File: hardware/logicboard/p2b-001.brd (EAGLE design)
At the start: 91 x 90 mm, 57 parts, among them IC1 74LS06N, IC2 4066N, J1 MKR, J2 GPIO, J3 Vcc, J4 RLY, J5 SPI, J7 DIN5, J8 DIN5, J9 DIN5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

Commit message: Added relay pad.
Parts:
- added A, B: (no value), wirepad:SMD1,27-2,54
- moved C1 1.00 mm to (26.0, 24.0)
- moved C2 1.00 mm to (26.0, 28.0)
- moved C3 1.00 mm to (26.0, 31.0)
- moved C4 1.00 mm to (26.0, 34.0)
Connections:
- net VOUTRAW: now also B.1
- net VOUTRAW2: now also A.1
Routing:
- net VIN: track 81.9 -> 142.1 mm, vias 6 -> 7
- net DTCT0: track 71.1 -> 112.8 mm, vias 3 -> 2
- net LED1: track 87.4 -> 122.5 mm, vias 5 -> 4
- net SCL: track 150.7 -> 179.9 mm, vias 7 -> 3
- net THS: track 108.5 -> 129.8 mm, vias 0 -> 3
- net MTSND: track 78.8 -> 98.6 mm, vias 1 -> 0
- net DTCT2: track 127.7 -> 108.9 mm, vias 2 -> 3
- net GPIO1: track 127.0 -> 108.8 mm, vias 2 -> 6
- net MISND: track 111.9 -> 94.0 mm, vias 2 -> 6
- net DTCT3: track 127.7 -> 109.9 mm
- net RX: track 83.1 -> 67.3 mm, vias 2 -> 3
- net D7GATE: track 139.7 -> 125.0 mm, vias 0 -> 4
- net MOSND: track 67.0 -> 52.5 mm, vias 0 -> 3
- net GPIO0: track 109.1 -> 94.8 mm, vias 2 -> 3
- net VCC: track 310.8 -> 324.5 mm, vias 4 -> 3
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
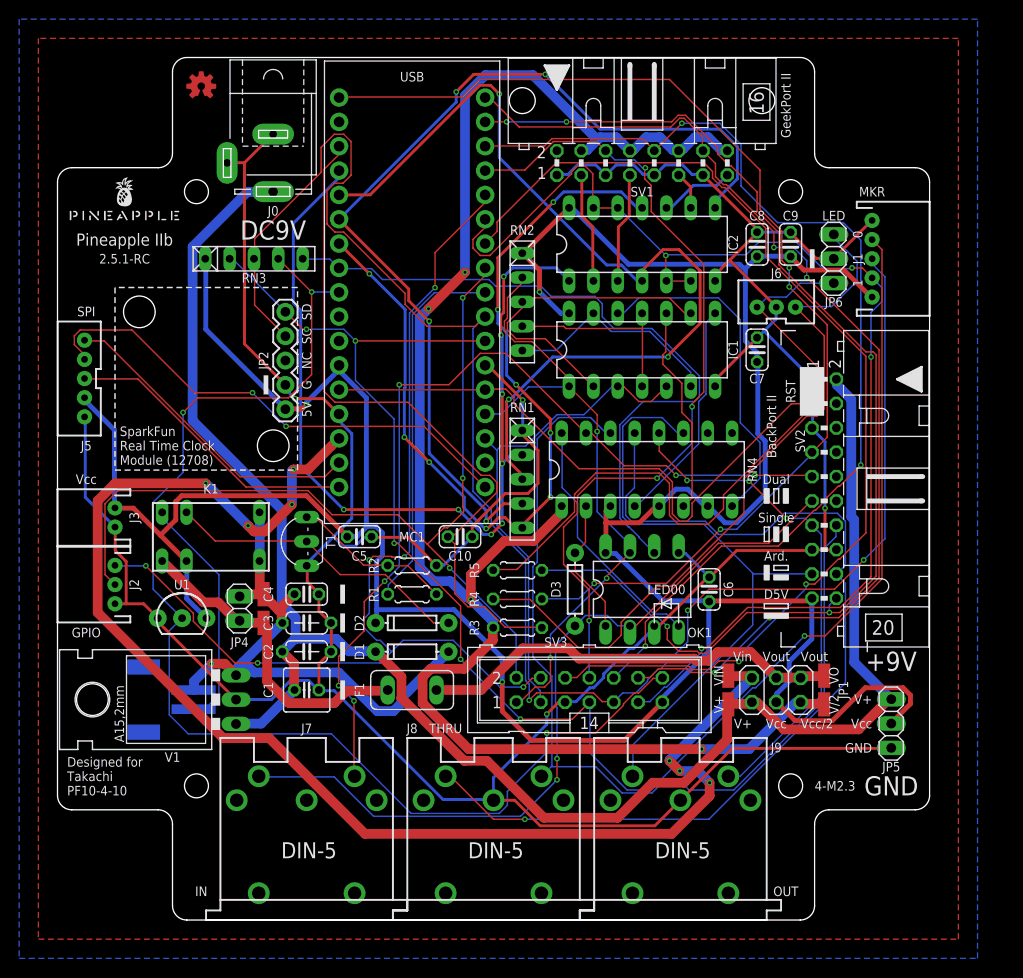
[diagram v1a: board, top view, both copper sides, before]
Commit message: Replaced ML connector with header pins.
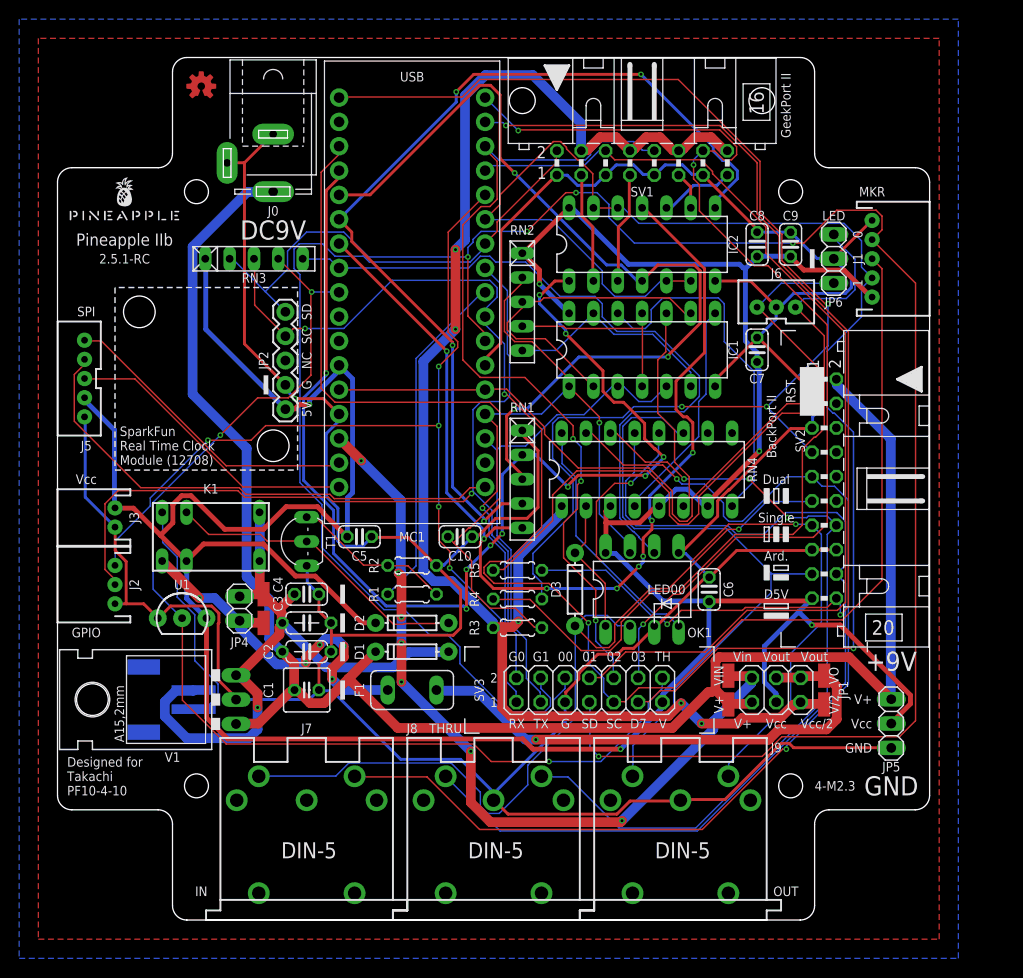
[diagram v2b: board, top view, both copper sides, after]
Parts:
- SV3: device con-ml:ML14 -> pinhead:2X07
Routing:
- net VIN: track 142.1 -> 83.7 mm
- net GND: track 375.9 -> 425.9 mm, vias 4 -> 1
- net VCC: track 324.5 -> 353.0 mm, vias 3 -> 5
- net ANLG0: track 93.8 -> 121.8 mm, vias 8 -> 10
- net SDA: track 167.5 -> 190.6 mm, vias 6 -> 5
- net D7GATE: track 125.0 -> 146.9 mm, vias 4 -> 1
- net DTCT2: track 108.9 -> 88.4 mm
- net MISND: track 94.0 -> 114.5 mm, vias 6 -> 2
- net DTCT1: track 85.9 -> 106.2 mm, vias 4 -> 0
- net SCL: track 179.9 -> 160.4 mm
- net MOSND: track 52.5 -> 71.6 mm, vias 3 -> 2
- net ANLG3: track 91.2 -> 108.5 mm, vias 9 -> 8
- net MTSND: track 98.6 -> 83.7 mm, vias 0 -> 3
- net LED0: track 116.3 -> 130.8 mm, vias 4 -> 3
- net VCC/2: track 172.4 -> 159.7 mm, vias 4 -> 5
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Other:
- board text added: "00"
- board text added: "01"
- board text added: "02"
- board text added: "03"
- board text added: "2"
- board text added: "D7"
- board text added: "G0"
- board text added: "G1"
- board text added: "RX"
- board text added: "TH"
- board text added: "TX"
- board text added: "V"

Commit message: Position of Tr.
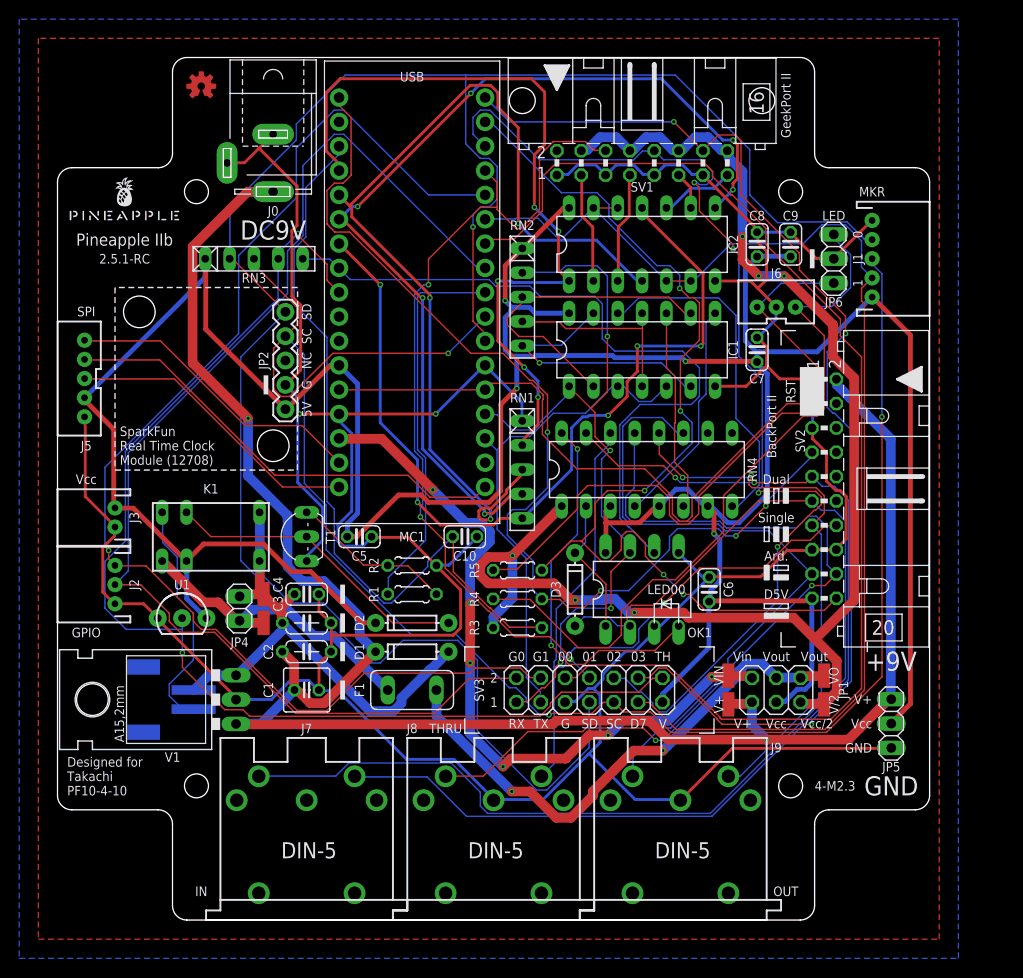
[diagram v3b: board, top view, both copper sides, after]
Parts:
- moved RN1 1.00 mm to (48.5, 47.0)
- moved C10 0.50 mm to (42.5, 40.0)
- moved RN2 0.50 mm to (48.5, 65.0)
- moved T1 0.50 mm to (26.0, 40.0)
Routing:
- net ANLG0: track 121.8 -> 81.4 mm, vias 10 -> 5
- net MIRTN: track 91.3 -> 123.7 mm, vias 1 -> 0
- net GPIO0: track 97.5 -> 127.5 mm, vias 1 -> 0
- net SDA: track 190.6 -> 216.7 mm, vias 5 -> 1
- net DTCT2: track 88.4 -> 114.0 mm, vias 3 -> 4
- net DTCT0: track 103.5 -> 126.7 mm
- net LED0: track 130.8 -> 108.2 mm, vias 3 -> 4
- net D7GATE: track 146.9 -> 124.6 mm, vias 1 -> 0
- net GPIO1: track 109.3 -> 130.7 mm, vias 5 -> 1
- net SCL: track 160.4 -> 180.0 mm
- net DTCT1: track 106.2 -> 88.1 mm, vias 0 -> 3
- net ANLG3: track 108.5 -> 90.8 mm, vias 8 -> 5
- net GND: track 425.9 -> 410.2 mm, vias 1 -> 2
- net VCC: track 353.0 -> 368.7 mm, vias 5 -> 4
- net MTRTN: track 102.2 -> 87.8 mm, vias 0 -> 2
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
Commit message: Changed silk of BackPort II.
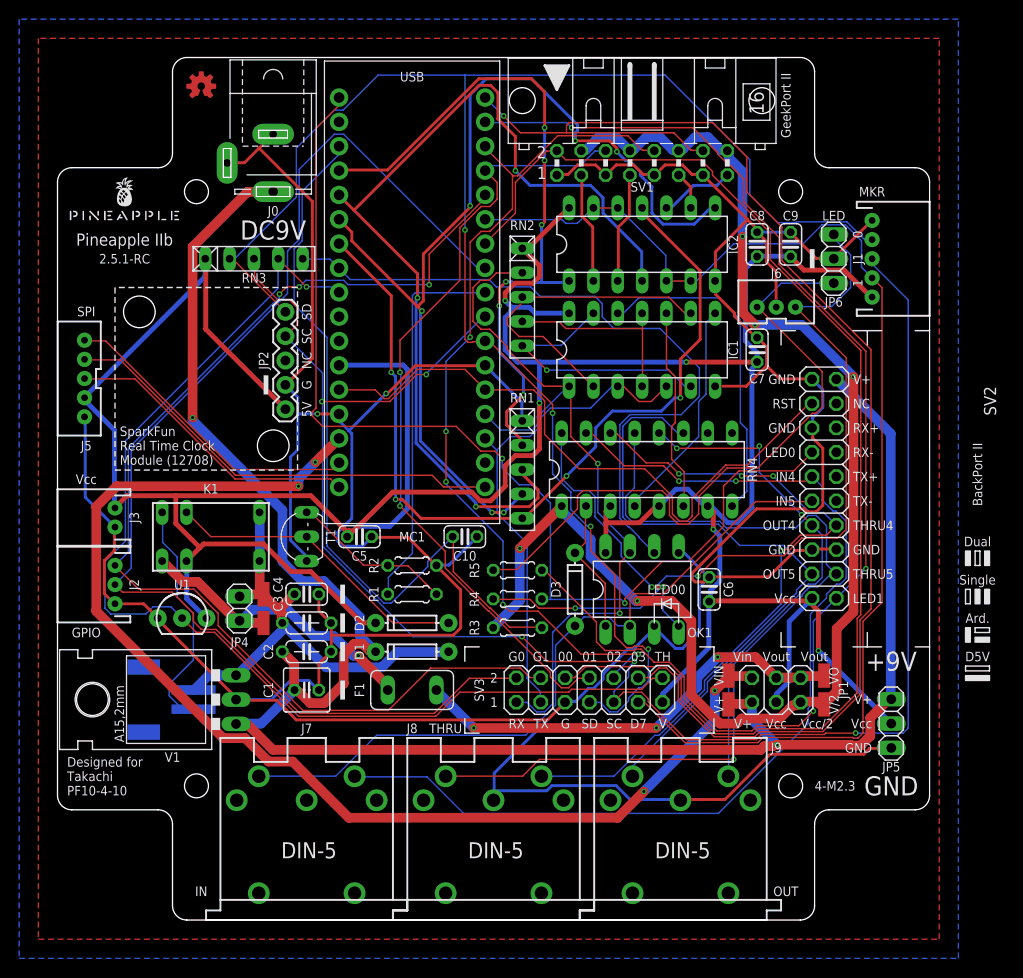
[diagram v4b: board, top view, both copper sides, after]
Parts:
- SV2: device con-ml:ML20L -> pinhead:2X10
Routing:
- net VIN: track 76.5 -> 125.1 mm, vias 6 -> 4
- net MIRTN: track 123.7 -> 75.8 mm
- net GND: track 410.2 -> 449.7 mm
- net SDA: track 216.7 -> 177.7 mm, vias 1 -> 4
- net LED1: track 104.8 -> 131.4 mm, vias 5 -> 3
- net DTCT2: track 114.0 -> 92.1 mm, vias 4 -> 5
- net DTCT3: track 119.9 -> 137.8 mm, vias 3 -> 1
- net GPIO1: track 130.7 -> 117.3 mm, vias 1 -> 3
- net MNTRA: track 39.9 -> 26.8 mm
- net ANLG0: track 81.4 -> 72.5 mm, vias 5 -> 6
- net VOUT: track 55.4 -> 46.8 mm, vias 2 -> 3
- net THS: track 123.5 -> 116.9 mm, vias 2 -> 1
- net VCC: track 368.7 -> 362.9 mm, vias 4 -> 5
- net V+: track 199.6 -> 204.7 mm
- net DTCT1: track 88.1 -> 83.1 mm, vias 3 -> 2
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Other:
- board text added: "IN4"
- board text added: "IN5"
- board text added: "LED0"
- board text added: "LED1"
- board text added: "OUT4"
- board text added: "OUT5"
- board text added: "RX+"
- board text added: "RX-"
- board text added: "THRU4"
- board text added: "THRU5"
- board text added: "TX+"
- board text added: "TX-"
